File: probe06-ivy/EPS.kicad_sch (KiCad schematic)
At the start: 30 parts, among them J1 USB_B_Micro, SW2 SW_SPDT, U2 MP1584EN, U3 AMS1117-3.3

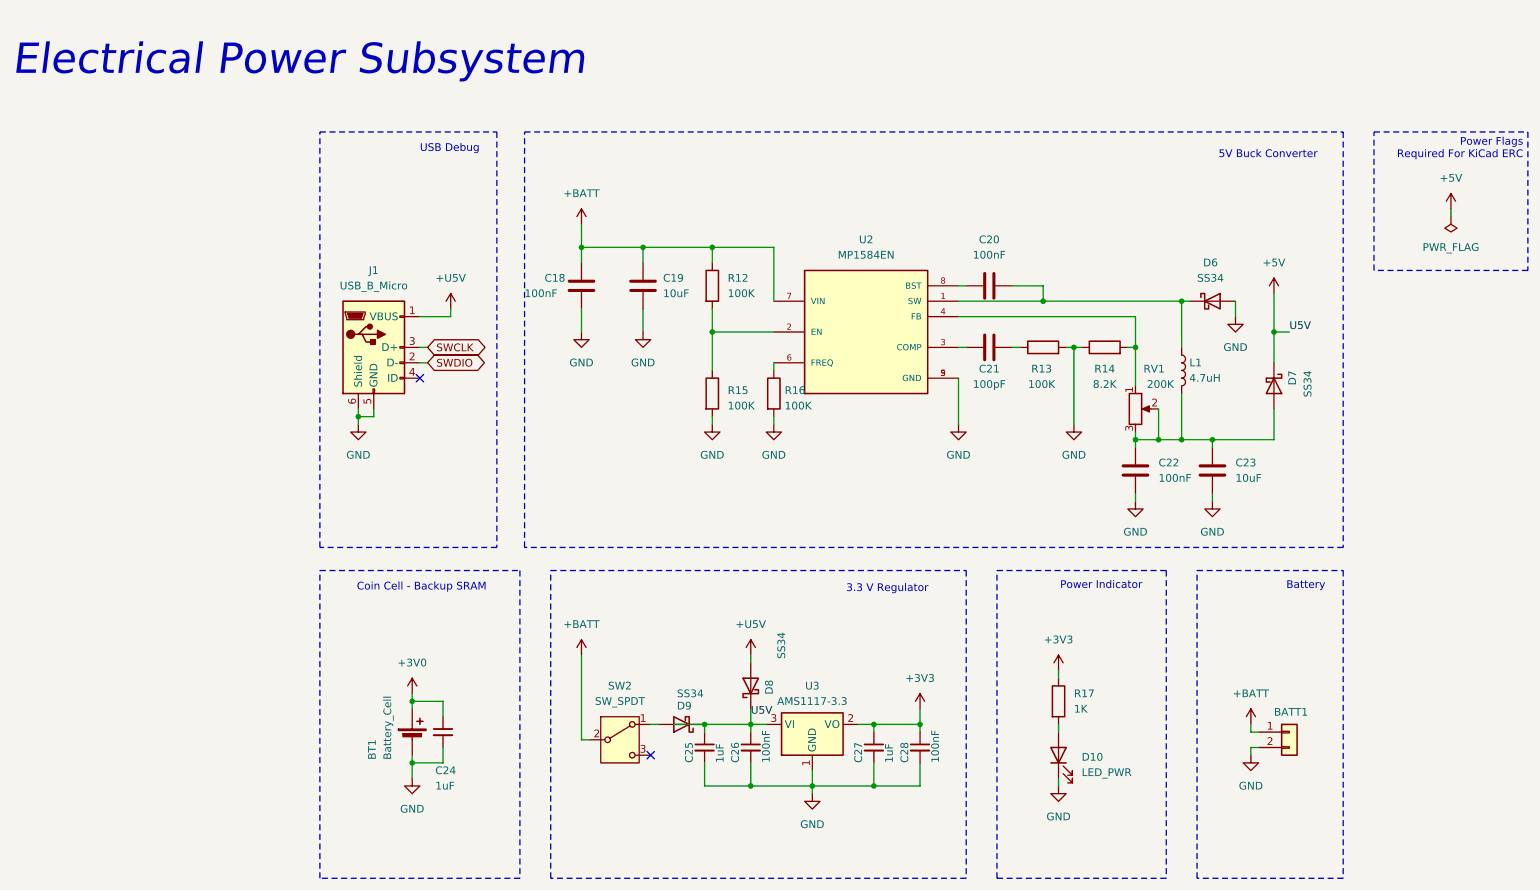
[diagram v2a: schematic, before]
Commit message: Routing (2) - make the pcb edge cuts to suit mechanic requirements - route some components (power, usb debug, gps) progress 50%
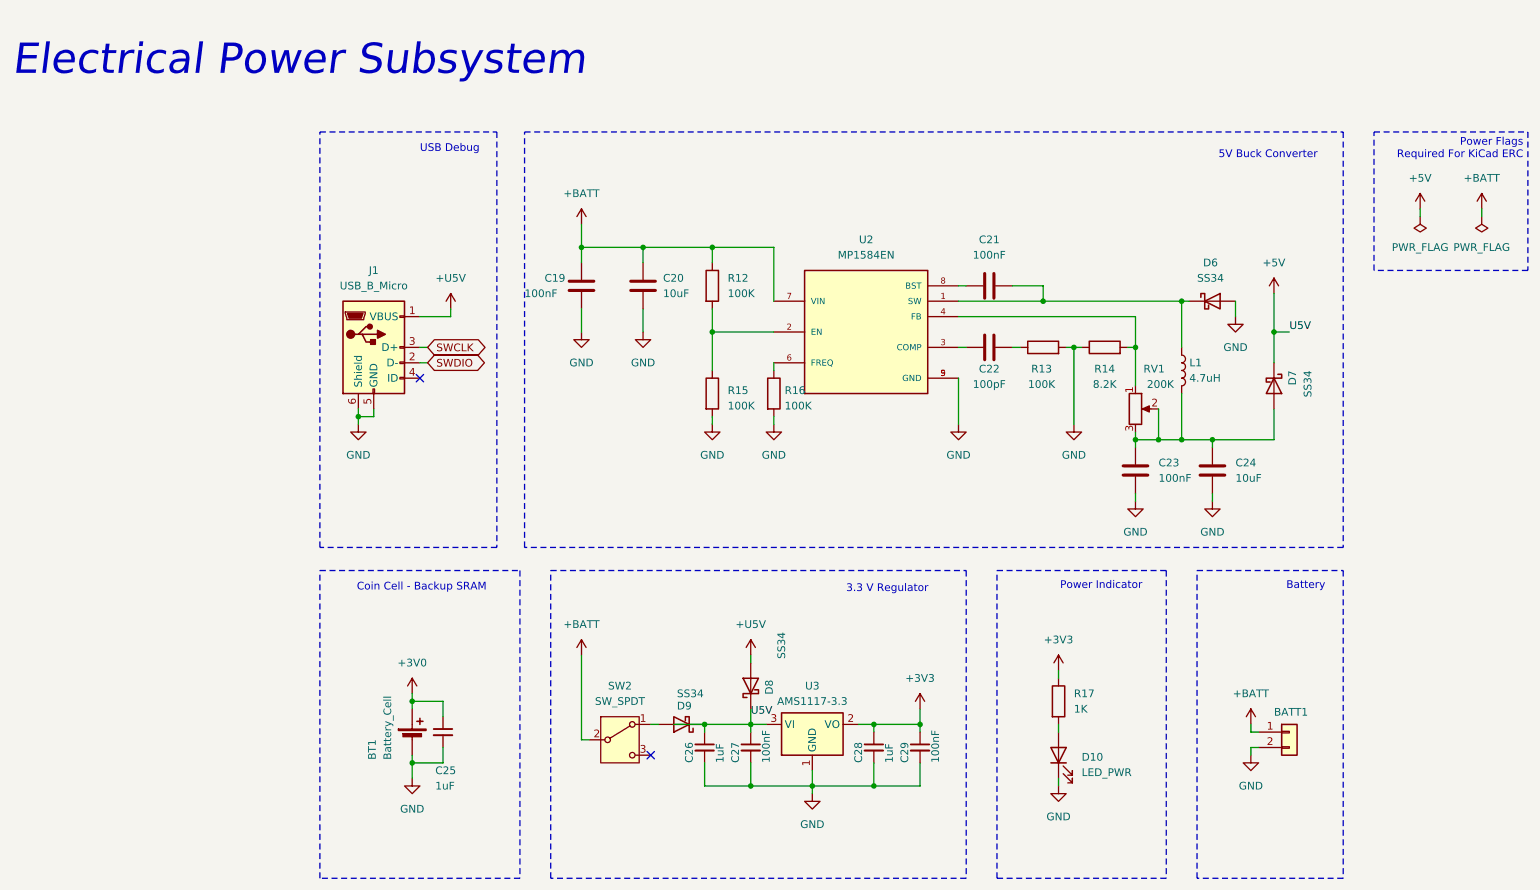
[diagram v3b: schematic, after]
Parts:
- C20: renamed from C19; footprint Capacitor_SMD:C_0805_2012Metric -> Capacitor_SMD:C_1206_3216Metric
- C24: renamed from C23; footprint Capacitor_SMD:C_0805_2012Metric -> Capacitor_SMD:C_1206_3216Metric
- C25: renamed from C24; footprint Capacitor_SMD:C_0805_2012Metric -> Capacitor_SMD:C_0603_1608Metric
- C26: renamed from C25; footprint Capacitor_SMD:C_0805_2012Metric -> Capacitor_SMD:C_0603_1608Metric
- C27: renamed from C26; footprint Capacitor_SMD:C_0805_2012Metric -> Capacitor_SMD:C_0603_1608Metric
- C28: renamed from C27; footprint Capacitor_SMD:C_0805_2012Metric -> Capacitor_SMD:C_0603_1608Metric
- C29: renamed from C28; footprint Capacitor_SMD:C_0805_2012Metric -> Capacitor_SMD:C_0603_1608Metric
- D10: footprint LED_SMD:LED_0805_2012Metric -> LED_SMD:LED_0603_1608Metric
- R17: footprint Resistor_SMD:R_0805_2012Metric -> Resistor_SMD:R_0603_1608Metric
- renumbered C18 to C19, C20 to C21, C21 to C22, C22 to C23
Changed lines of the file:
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@@
 	(wire
 		(pts
+			(xy 259.08 50.8) (xy 259.08 52.07)
+		)
+		(stroke
+			(width 0)
+			(type default)
+		)
+	)
+	(wire
+		(pts
 			(xy 158.75 146.05) (xy 148.59 146.05)
 		)
@@
 	(wire
 		(pts
-			(xy 254 52.07) (xy 254 50.8)
+			(xy 248.92 52.07) (xy 248.92 50.8)
 		)
 		(stroke
@@
 	)
 	(symbol
+		(lib_name "+BATT_1")
+		(lib_id "power:+BATT")
+		(at 259.08 50.8 0)
+		(unit 1)
+		(exclude_from_sim no)
+		(in_bom yes)
+		(on_board yes)
+		(dnp no)
+		(fields_autoplaced yes)
+		(property "Reference" "#PWR089"
+			(at 259.08 54.61 0)
+			(effects
+				(font
+					(size 1.27 1.27)
+				)
+				(hide yes)
+			)
+		)
+		(property "Value" "+BATT"
+			(at 259.08 45.72 0)
+			(effects
+				(font
+					(size 1.27 1.27)
+				)
+			)
+		)
+		(property "Footprint" ""
+			(at 259.08 50.8 0)
+			(effects
+				(font
+					(size 1.27 1.27)
+				)
+				(hide yes)
+			)
+		)
+		(property "Datasheet" ""
+			(at 259.08 50.8 0)
+			(effects
+				(font
+					(size 1.27 1.27)
+				)
+				(hide yes)
+			)
+		)
+		(property "Description" "Power symbol creates a global label with name \"+BATT\""
+			(at 259.08 50.8 0)
+			(effects
+				(font
+					(size 1.27 1.27)
+				)
+				(hide yes)
+			)
+		)
+		(pin "1"
+		)
+		(instances
+			(project "probe06-ivy"
+				(path "/8ec4aa67-98d5-4482-bf96-6c1e71ad8a74/9fa331a9-6a87-4974-bb86-bec099ef0d79"
+					(reference "#PWR089")
+					(unit 1)
+				)
+			)
+		)
+	)
+	(symbol
 		(lib_id "power:+5VA")
 		(at 138.43 124.46 0)
@@
 		(on_board yes)
 		(dnp no)
-		(property "Reference" "C27"
+		(property "Reference" "C28"
 			(at 156.21 142.24 90)
 			(effects
@@
 			)
 		)
-		(property "Footprint" "Capacitor_SMD:C_0805_2012Metric"
+		(property "Footprint" "Capacitor_SMD:C_0603_1608Metric"
 			(at 158.75 139.7 0)
 			(effects
@@
 			(project "probe06-ivy"
 				(path "/8ec4aa67-98d5-4482-bf96-6c1e71ad8a74/9fa331a9-6a87-4974-bb86-bec099ef0d79"
-					(reference "C27")
+					(reference "C28")
 					(unit 1)
 				)
@@
 			)
 		)
-		(property "Footprint" "Resistor_SMD:R_0805_2012Metric"
+		(property "Footprint" "Resistor_SMD:R_0603_1608Metric"
 			(at 187.452 132.08 90)
 			(effects
@@
 		(dnp no)
 		(fields_autoplaced yes)
-		(property "Reference" "C22"
+		(property "Reference" "C23"
 			(at 205.74 92.7099 0)
 			(effects
@@
 			(project "probe06-ivy"
 				(path "/8ec4aa67-98d5-4482-bf96-6c1e71ad8a74/9fa331a9-6a87-4974-bb86-bec099ef0d79"
-					(reference "C22")
+					(reference "C23")
 					(unit 1)
 				)
@@
 		(on_board yes)
 		(dnp no)
-		(property "Reference" "C21"
+		(property "Reference" "C22"
 			(at 177.8 77.216 90)
 			(effects
@@
 			(project "probe06-ivy"
 				(path "/8ec4aa67-98d5-4482-bf96-6c1e71ad8a74/9fa331a9-6a87-4974-bb86-bec099ef0d79"
-					(reference "C21")
+					(reference "C22")
 					(unit 1)
 				)
@@
 		(on_board yes)
 		(dnp no)
-		(property "Reference" "C18"
+		(property "Reference" "C19"
 			(at 104.394 62.23 0)
 			(effects
@@
 			(project ""
 				(path "/8ec4aa67-98d5-4482-bf96-6c1e71ad8a74/9fa331a9-6a87-4974-bb86-bec099ef0d79"
-					(reference "C18")
+					(reference "C19")
 					(unit 1)
 				)
@@
 		(dnp no)
 		(fields_autoplaced yes)
-		(property "Reference" "C20"
+		(property "Reference" "C21"
 			(at 177.8 55.88 90)
 			(effects
@@
 			(project "probe06-ivy"
 				(path "/8ec4aa67-98d5-4482-bf96-6c1e71ad8a74/9fa331a9-6a87-4974-bb86-bec099ef0d79"
-					(reference "C20")
+					(reference "C21")
 					(unit 1)
 				)
@@
 		(on_board yes)
 		(dnp no)
-		(property "Reference" "C24"
+		(property "Reference" "C25"
 			(at 86.36 143.51 0)
 			(effects
@@
 			)
 		)
-		(property "Footprint" "Capacitor_SMD:C_0805_2012Metric"
+		(property "Footprint" "Capacitor_SMD:C_0603_1608Metric"
 			(at 87.63 137.16 0)
 			(effects
@@
 			(project "probe06-ivy"
 				(path "/8ec4aa67-98d5-4482-bf96-6c1e71ad8a74/9fa331a9-6a87-4974-bb86-bec099ef0d79"
-					(reference "C24")
+					(reference "C25")
 					(unit 1)
 				)
@@
 		(on_board yes)
 		(dnp no)
-		(property "Reference" "C19"
+		(property "Reference" "C20"
 			(at 123.952 62.23 0)
 			(effects
@@
 			)
 		)
-		(property "Footprint" "Capacitor_SMD:C_0805_2012Metric"
+		(property "Footprint" "Capacitor_SMD:C_1206_3216Metric"
 			(at 121.6152 67.31 0)
 			(effects
@@
 			(project "probe06-ivy"
 				(path "/8ec4aa67-98d5-4482-bf96-6c1e71ad8a74/9fa331a9-6a87-4974-bb86-bec099ef0d79"
-					(reference "C19")
+					(reference "C20")
 					(unit 1)
 				)
@@
 		(on_board yes)
 		(dnp no)
-		(property "Reference" "C28"
+		(property "Reference" "C29"
 			(at 163.83 142.24 90)
 			(effects
@@
 			)
 		)
-		(property "Footprint" "Capacitor_SMD:C_0805_2012Metric"
+		(property "Footprint" "Capacitor_SMD:C_0603_1608Metric"
 			(at 166.37 139.7 0)
 			(effects
@@
 			(project "probe06-ivy"
 				(path "/8ec4aa67-98d5-4482-bf96-6c1e71ad8a74/9fa331a9-6a87-4974-bb86-bec099ef0d79"
-					(reference "C28")
+					(reference "C29")
+					(unit 1)
+				)
+			)
+		)
+	)
+	(symbol
+		(lib_id "power:PWR_FLAG")
+		(at 259.08 52.07 180)
+		(unit 1)
+		(exclude_from_sim no)
+		(in_bom yes)
+		(on_board yes)
+		(dnp no)
+		(fields_autoplaced yes)
+		(property "Reference" "#FLG02"
+			(at 259.08 53.975 0)
+			(effects
+				(font
+					(size 1.27 1.27)
+				)
+				(hide yes)
+			)
+		)
+		(property "Value" "PWR_FLAG"
+			(at 259.08 57.15 0)
+			(effects
+				(font
+					(size 1.27 1.27)
+				)
+			)
+		)
+		(property "Footprint" ""
+			(at 259.08 52.07 0)
+			(effects
+				(font
+					(size 1.27 1.27)
+				)
+				(hide yes)
+			)
+		)
+		(property "Datasheet" "~"
+			(at 259.08 52.07 0)
+			(effects
+				(font
+					(size 1.27 1.27)
+				)
+				(hide yes)
+			)
+		)
+		(property "Description" "Special symbol for telling ERC where power comes from"
+			(at 259.08 52.07 0)
+			(effects
+				(font
+					(size 1.27 1.27)
+				)
+				(hide yes)
+			)
+		)
+		(pin "1"
+		)
+		(instances
+			(project "probe06-ivy"
+				(path "/8ec4aa67-98d5-4482-bf96-6c1e71ad8a74/9fa331a9-6a87-4974-bb86-bec099ef0d79"
+					(reference "#FLG02")
 					(unit 1)
 				)
@@
 		(dnp no)
 		(fields_autoplaced yes)
-		(property "Reference" "C23"
+		(property "Reference" "C24"
 			(at 218.44 92.7099 0)
 			(effects
@@
 			)
 		)
-		(property "Footprint" "Capacitor_SMD:C_0805_2012Metric"
+		(property "Footprint" "Capacitor_SMD:C_1206_3216Metric"
 			(at 215.5952 97.79 0)
 			(effects
@@
 			(project "probe06-ivy"
 				(path "/8ec4aa67-98d5-4482-bf96-6c1e71ad8a74/9fa331a9-6a87-4974-bb86-bec099ef0d79"
-					(reference "C23")
+					(reference "C24")
 					(unit 1)
 				)
@@
 	(symbol
 		(lib_id "power:PWR_FLAG")
-		(at 254 52.07 180)
+		(at 248.92 52.07 180)
 		(unit 1)
 		(exclude_from_sim no)
@@
 		(fields_autoplaced yes)
 		(property "Reference" "#FLG04"
-			(at 254 53.975 0)
+			(at 248.92 53.975 0)
 			(effects
 				(font
@@
 		)
 		(property "Value" "PWR_FLAG"
-			(at 254 57.15 0)
+			(at 248.92 57.15 0)
 			(effects
 				(font
@@
 		)
 		(property "Footprint" ""
-			(at 254 52.07 0)
+			(at 248.92 52.07 0)
 			(effects
 				(font
@@
 		)
 		(property "Datasheet" "~"
-			(at 254 52.07 0)
+			(at 248.92 52.07 0)
 			(effects
 				(font
@@
 		)
 		(property "Description" "Special symbol for telling ERC where power comes from"
-			(at 254 52.07 0)
+			(at 248.92 52.07 0)
 			(effects
 				(font
@@
 			)
 		)
-		(property "Footprint" "LED_SMD:LED_0805_2012Metric"
+		(property "Footprint" "LED_SMD:LED_0603_1608Metric"
 			(at 189.23 140.97 0)
 			(effects
@@
 	(symbol
 		(lib_id "power:+5V")
-		(at 254 50.8 0)
+		(at 248.92 50.8 0)
 		(unit 1)
 		(exclude_from_sim no)
@@
 		(fields_autoplaced yes)
 		(property "Reference" "#PWR023"
-			(at 254 54.61 0)
+			(at 248.92 54.61 0)
 			(effects
 				(font
@@
 		)
 		(property "Value" "+5V"
-			(at 254 45.72 0)
+			(at 248.92 45.72 0)
 			(effects
 				(font
@@
 		)
 		(property "Footprint" ""
-			(at 254 50.8 0)
+			(at 248.92 50.8 0)
 			(effects
 				(font
@@
 		)
 		(property "Datasheet" ""
-			(at 254 50.8 0)
+			(at 248.92 50.8 0)
 			(effects
 				(font
@@
 		)
 		(property "Description" "Power symbol creates a global label with name \"+5V\""
-			(at 254 50.8 0)
+			(at 248.92 50.8 0)
 			(effects
 				(font
@@
 		(on_board yes)
 		(dnp no)
-		(property "Reference" "C26"
+		(property "Reference" "C27"
 			(at 135.89 142.24 90)
 			(effects
@@
 			)
 		)
-		(property "Footprint" "Capacitor_SMD:C_0805_2012Metric"
+		(property "Footprint" "Capacitor_SMD:C_0603_1608Metric"
 			(at 138.43 139.7 0)
 			(effects
@@
 			(project "probe06-ivy"
 				(path "/8ec4aa67-98d5-4482-bf96-6c1e71ad8a74/9fa331a9-6a87-4974-bb86-bec099ef0d79"
-					(reference "C26")
+					(reference "C27")
 					(unit 1)
 				)
@@
 		(on_board yes)
 		(dnp no)
-		(property "Reference" "C25"
+		(property "Reference" "C26"
 			(at 128.27 142.24 90)
 			(effects
@@
 			)
 		)
-		(property "Footprint" "Capacitor_SMD:C_0805_2012Metric"
+		(property "Footprint" "Capacitor_SMD:C_0603_1608Metric"
 			(at 130.81 139.7 0)
 			(effects
@@
 			(project "probe06-ivy"
 				(path "/8ec4aa67-98d5-4482-bf96-6c1e71ad8a74/9fa331a9-6a87-4974-bb86-bec099ef0d79"
-					(reference "C25")
+					(reference "C26")
 					(unit 1)
 				)
